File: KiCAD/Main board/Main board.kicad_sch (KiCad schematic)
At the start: 29 parts, among them J1 Conn_01x03, J10 Conn_01x03, J11 Conn_01x03, J12 Conn_01x03, J13 Conn_01x02, J14 Conn_01x02, J15 Conn_01x06, J16 Conn_01x02, J17 Conn_01x02, J18 Conn_01x05, J2 Conn_01x03, J3 Conn_01x02, J4 Conn_01x02, J5 Conn_01x03, J6 Conn_01x02, J7 Conn_01x03, J8 Conn_01x02, J9 Conn_01x03

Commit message: Ad good as finilized the main board schematic
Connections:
- net ADC_CH3_4/VU_G1_CH4: now reaches J18.2 (Pin_2)
- net ADC_CH3_4/VU_G2_CH4: now reaches J18.3 (Pin_3)
- net ADC_CH3_4/VU_O1_CH4: now reaches J18.4 (Pin_4)
- net ADC_CH3_4/VU_R1_CH4: now reaches J18.5 (Pin_5)
- net ADC_CH3_4/VU_G1_CH3: now reaches J18.2 (Pin_2)
- net ADC_CH3_4/VU_G2_CH3: now reaches J18.3 (Pin_3)
- net ADC_CH3_4/VU_O1_CH3: now reaches J18.4 (Pin_4)
- net ADC_CH3_4/VU_R1_CH3: now reaches J18.5 (Pin_5)
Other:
- sheet ADC_CH1_2 ports: added none; removed ~{RST_ADC_CH1_2}
- sheet ADC_CH3_4 ports: added BCK_ADC_CH3_4, DATA_ADC_CH3_4, LRCK_ADC_CH3_4, SCKI_ADC_CH3_4, VU_G1_CH3, VU_G1_CH4, VU_G2_CH3, VU_G2_CH4, VU_O1_CH3, VU_O1_CH4, VU_R1_CH3, VU_R1_CH4; removed none
- sheet FPGA ports: added BCK_ADC_CH3_4, DATA_ADC_CH3_4, LRCK_ADC_CH3_4, SCKI_ADC_CH3_4; removed ~{RST_ADC_CH1_2}
- note added: "-Use Panasonic ERA-8A series for audio path resistors -Use C0G MLCC capacitors for audio path capacitors"
- note added: "Check all custom symbols and footprints with someone else"
- moved on the sheet: H1, H2, H3, H4, H5, H6, H7, H8, J13, J14, J15

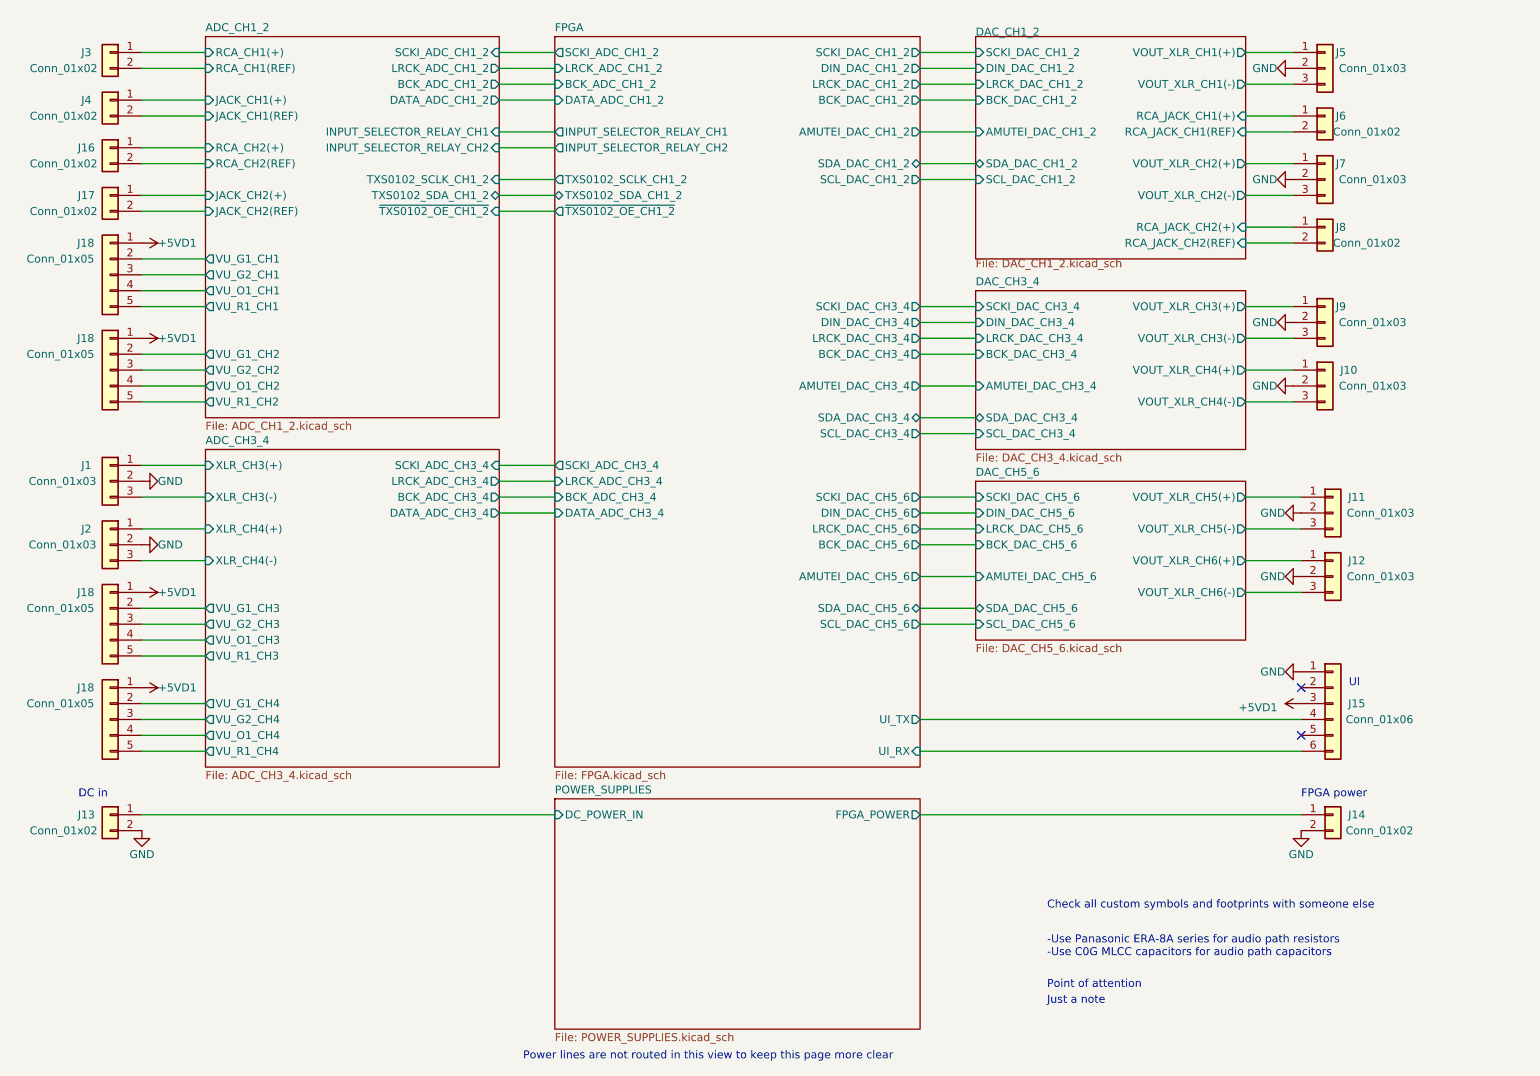
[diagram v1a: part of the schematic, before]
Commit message: Finalizer main board schematic exept passive order links. Schematic ready for review
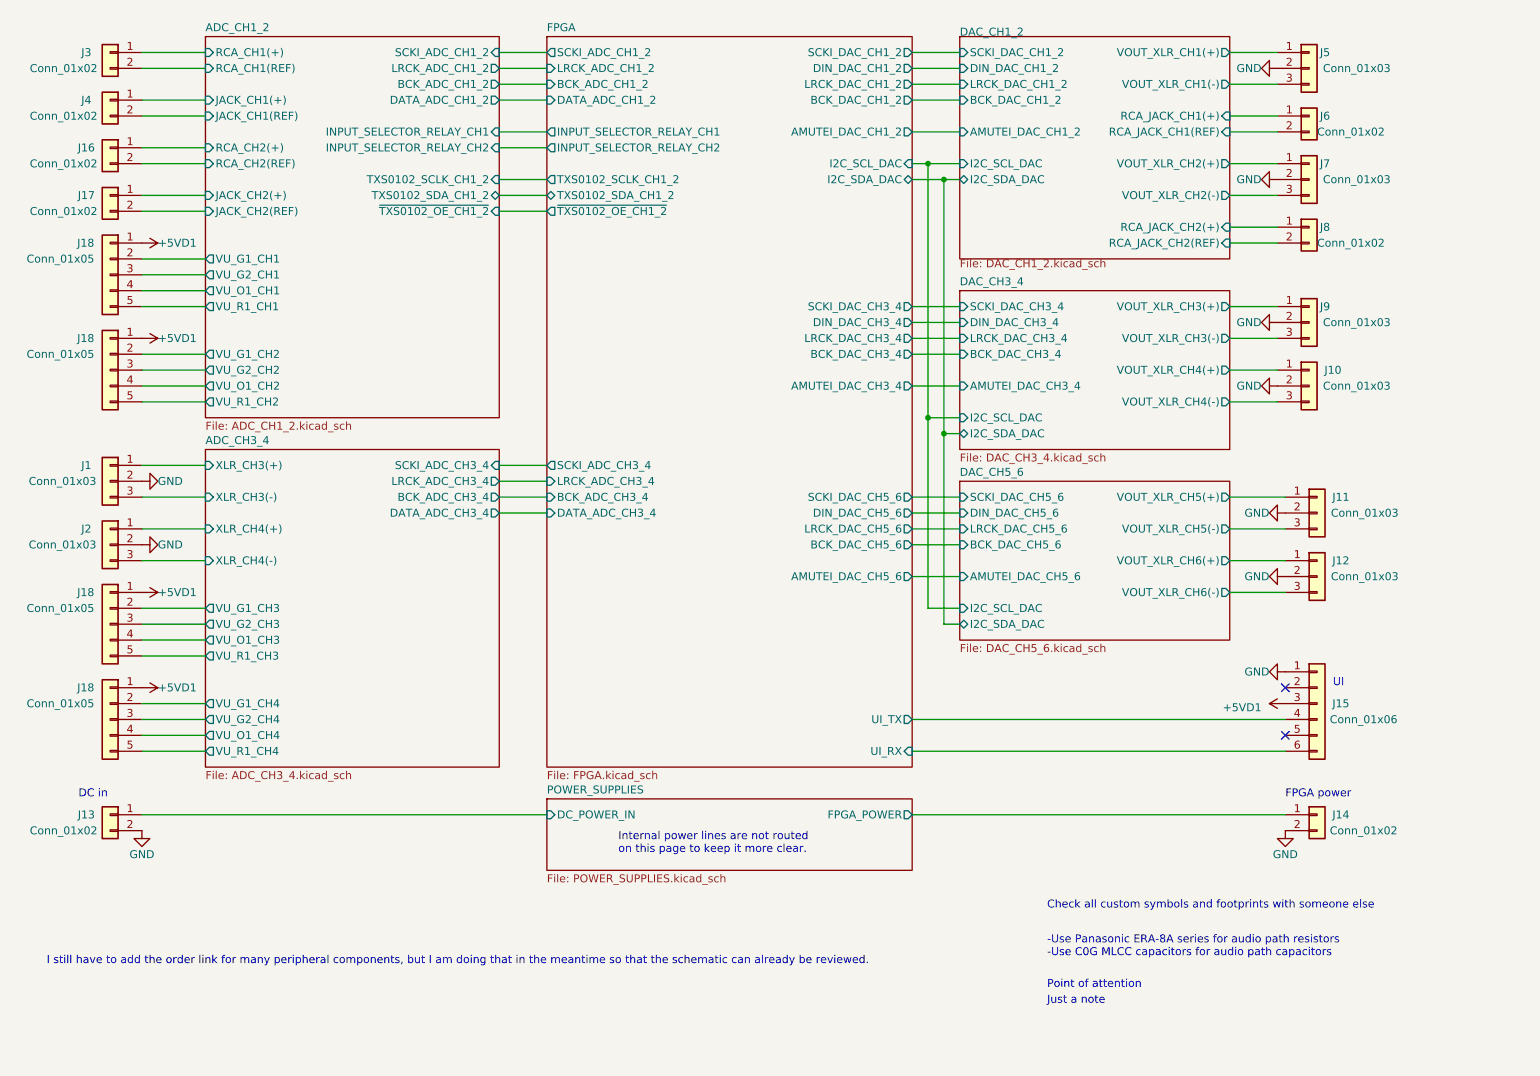
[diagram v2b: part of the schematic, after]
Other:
- sheet DAC_CH1_2 ports: added I2C_SCL_DAC, I2C_SDA_DAC; removed SCL_DAC_CH1_2, SDA_DAC_CH1_2
- sheet DAC_CH3_4 ports: added I2C_SCL_DAC, I2C_SDA_DAC; removed SCL_DAC_CH3_4, SDA_DAC_CH3_4
- sheet DAC_CH5_6 ports: added I2C_SCL_DAC, I2C_SDA_DAC; removed SCL_DAC_CH5_6, SDA_DAC_CH5_6
- sheet FPGA ports: added I2C_SCL_DAC, I2C_SDA_DAC; removed SCL_DAC_CH1_2, SCL_DAC_CH3_4, SCL_DAC_CH5_6, SDA_DAC_CH1_2, SDA_DAC_CH3_4, SDA_DAC_CH5_6
- note added: "I still have to add the order link for many peripheral components, but I am doing that in the meantime so that the schematic can already be reviewed."
- note added: "Internal power lines are not routed on this page to keep it more clear."
- note removed: "Power lines are not routed in this view to keep this page more clear"
- moved on the sheet: J10, J11, J12, J14, J15, J5, J6, J7, J8, J9

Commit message: Added component links to main board schematic
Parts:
- J1, J10, J11, J12, J16, J17, J2, J3, J4, J5, J6, J7, J8, J9: Cable (none) -> https://www.tinytronics.nl/shop/nl/kabels-en-connectoren/ka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
- J15: Cable (none) -> https://www.tinytronics.nl/shop/nl/kabels-en-connectoren/ka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; Datasheet cable https://www.tinytronics.nl/shop/nl/kabels-en-connectoren/ka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 -> (none)
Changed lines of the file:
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@@
       (effects (font (size 1.27 1.27)) hide)
     )
-    (property "Datasheet" "~" (at 27.94 87.63 0)
+    (property "Datasheet" "https://www.tinytronics.nl/shop/nl/kabels-en-connectoren/connectoren/jst-compatible/jst-ph-3p-compatible-printplaatconnector-male" (at 27.94 87.63 0)
+      (effects (font (size 1.27 1.27)) hide)
+    )
+    (property "Cable" "https://www.tinytronics.nl/shop/nl/kabels-en-connectoren/kabels-en-adapters/jst-compatible/jst-ph-3p-compatible-kabel-20cm" (at 27.94 87.63 0)
       (effects (font (size 1.27 1.27)) hide)
     )
@@
       (effects (font (size 1.27 1.27)) hide)
     )
-    (property "Datasheet" "~" (at 27.94 19.05 0)
+    (property "Datasheet" "https://www.tinytronics.nl/shop/nl/kabels-en-connectoren/connectoren/jst-compatible/jst-ph-2p-compatible-printplaatconnector-male" (at 27.94 19.05 0)
+      (effects (font (size 1.27 1.27)) hide)
+    )
+    (property "Cable" "https://www.tinytronics.nl/shop/nl/kabels-en-connectoren/kabels-en-adapters/jst-compatible/jst-2.0mm-connector-met-kabel-ph2.0-2-pins" (at 27.94 19.05 0)
       (effects (font (size 1.27 1.27)) hide)
     )
@@
       (effects (font (size 1.27 1.27)) hide)
     )
-    (property "Datasheet" "~" (at 219.71 62.23 0)
+    (property "Datasheet" "https://www.tinytronics.nl/shop/nl/kabels-en-connectoren/connectoren/jst-compatible/jst-ph-3p-compatible-printplaatconnector-male" (at 219.71 62.23 0)
+      (effects (font (size 1.27 1.27)) hide)
+    )
+    (property "Cable" "https://www.tinytronics.nl/shop/nl/kabels-en-connectoren/kabels-en-adapters/jst-compatible/jst-ph-3p-compatible-kabel-20cm" (at 219.71 62.23 0)
       (effects (font (size 1.27 1.27)) hide)
     )
@@
       (effects (font (size 1.27 1.27)) hide)
     )
-    (property "Datasheet" "~" (at 219.71 29.21 0)
+    (property "Datasheet" "https://www.tinytronics.nl/shop/nl/kabels-en-connectoren/connectoren/jst-compatible/jst-ph-2p-compatible-printplaatconnector-male" (at 219.71 29.21 0)
+      (effects (font (size 1.27 1.27)) hide)
+    )
+    (property "Cable" "https://www.tinytronics.nl/shop/nl/kabels-en-connectoren/kabels-en-adapters/jst-compatible/jst-2.0mm-connector-met-kabel-ph2.0-2-pins" (at 219.71 29.21 0)
       (effects (font (size 1.27 1.27)) hide)
     )
@@
       (effects (font (size 1.27 1.27)) hide)
     )
-    (property "Datasheet" "~" (at 27.94 97.79 0)
+    (property "Datasheet" "https://www.tinytronics.nl/shop/nl/kabels-en-connectoren/connectoren/jst-compatible/jst-ph-3p-compatible-printplaatconnector-male" (at 27.94 97.79 0)
+      (effects (font (size 1.27 1.27)) hide)
+    )
+    (property "Cable" "https://www.tinytronics.nl/shop/nl/kabels-en-connectoren/kabels-en-adapters/jst-compatible/jst-ph-3p-compatible-kabel-20cm" (at 27.94 97.79 0)
       (effects (font (size 1.27 1.27)) hide)
     )
@@
       (effects (font (size 1.27 1.27)) hide)
     )
-    (property "Datasheet" "~" (at 27.94 34.29 0)
+    (property "Datasheet" "https://www.tinytronics.nl/shop/nl/kabels-en-connectoren/connectoren/jst-compatible/jst-ph-2p-compatible-printplaatconnector-male" (at 27.94 34.29 0)
+      (effects (font (size 1.27 1.27)) hide)
+    )
+    (property "Cable" "https://www.tinytronics.nl/shop/nl/kabels-en-connectoren/kabels-en-adapters/jst-compatible/jst-2.0mm-connector-met-kabel-ph2.0-2-pins" (at 27.94 34.29 0)
       (effects (font (size 1.27 1.27)) hide)
     )
@@
       (effects (font (size 1.27 1.27)) hide)
     )
-    (property "Datasheet" "~" (at 219.71 39.37 0)
+    (property "Datasheet" "https://www.tinytronics.nl/shop/nl/kabels-en-connectoren/connectoren/jst-compatible/jst-ph-3p-compatible-printplaatconnector-male" (at 219.71 39.37 0)
+      (effects (font (size 1.27 1.27)) hide)
+    )
+    (property "Cable" "https://www.tinytronics.nl/shop/nl/kabels-en-connectoren/kabels-en-adapters/jst-compatible/jst-ph-3p-compatible-kabel-20cm" (at 219.71 39.37 0)
       (effects (font (size 1.27 1.27)) hide)
     )
@@
       (effects (font (size 1.27 1.27)) hide)
     )
-    (property "Datasheet" "~" (at 219.71 46.99 0)
+    (property "Datasheet" "https://www.tinytronics.nl/shop/nl/kabels-en-connectoren/connectoren/jst-compatible/jst-ph-2p-compatible-printplaatconnector-male" (at 219.71 46.99 0)
+      (effects (font (size 1.27 1.27)) hide)
+    )
+    (property "Cable" "https://www.tinytronics.nl/shop/nl/kabels-en-connectoren/kabels-en-adapters/jst-compatible/jst-2.0mm-connector-met-kabel-ph2.0-2-pins" (at 219.71 46.99 0)
       (effects (font (size 1.27 1.27)) hide)
     )
@@
       (effects (font (size 1.27 1.27)) hide)
     )
-    (property "Datasheet cable" "https://www.tinytronics.nl/shop/nl/kabels-en-connectoren/kabels-en-adapters/jst-compatible/kabel-voor-stappenmotor-4-pin-jst-xh-naar-6-pin-jst-ph-motoraansluiting-20cm" (at 220.98 123.19 0)
+    (property "Cable" "https://www.tinytronics.nl/shop/nl/kabels-en-connectoren/kabels-en-adapters/jst-compatible/kabel-voor-stappenmotor-4-pin-jst-xh-naar-6-pin-jst-ph-motoraansluiting-20cm" (at 220.98 123.19 0)
       (effects (font (size 1.27 1.27)) hide)
     )
@@
       (effects (font (size 1.27 1.27)) hide)
     )
-    (property "Datasheet" "~" (at 219.71 72.39 0)
+    (property "Datasheet" "https://www.tinytronics.nl/shop/nl/kabels-en-connectoren/connectoren/jst-compatible/jst-ph-3p-compatible-printplaatconnector-male" (at 219.71 72.39 0)
+      (effects (font (size 1.27 1.27)) hide)
+    )
+    (property "Cable" "https://www.tinytronics.nl/shop/nl/kabels-en-connectoren/kabels-en-adapters/jst-compatible/jst-ph-3p-compatible-kabel-20cm" (at 219.71 72.39 0)
       (effects (font (size 1.27 1.27)) hide)
     )
@@
       (effects (font (size 1.27 1.27)) hide)
     )
-    (property "Datasheet" "~" (at 220.98 102.87 0)
+    (property "Datasheet" "https://www.tinytronics.nl/shop/nl/kabels-en-connectoren/connectoren/jst-compatible/jst-ph-3p-compatible-printplaatconnector-male" (at 220.98 102.87 0)
+      (effects (font (size 1.27 1.27)) hide)
+    )
+    (property "Cable" "https://www.tinytronics.nl/shop/nl/kabels-en-connectoren/kabels-en-adapters/jst-compatible/jst-ph-3p-compatible-kabel-20cm" (at 220.98 102.87 0)
       (effects (font (size 1.27 1.27)) hide)
     )
@@
       (effects (font (size 1.27 1.27)) hide)
     )
-    (property "Datasheet" "~" (at 219.71 21.59 0)
+    (property "Datasheet" "https://www.tinytronics.nl/shop/nl/kabels-en-connectoren/connectoren/jst-compatible/jst-ph-3p-compatible-printplaatconnector-male" (at 219.71 21.59 0)
+      (effects (font (size 1.27 1.27)) hide)
+    )
+    (property "Cable" "https://www.tinytronics.nl/shop/nl/kabels-en-connectoren/kabels-en-adapters/jst-compatible/jst-ph-3p-compatible-kabel-20cm" (at 219.71 21.59 0)
       (effects (font (size 1.27 1.27)) hide)
     )
@@
       (effects (font (size 1.27 1.27)) hide)
     )
-    (property "Datasheet" "~" (at 220.98 92.71 0)
+    (property "Datasheet" "https://www.tinytronics.nl/shop/nl/kabels-en-connectoren/connectoren/jst-compatible/jst-ph-3p-compatible-printplaatconnector-male" (at 220.98 92.71 0)
+      (effects (font (size 1.27 1.27)) hide)
+    )
+    (property "Cable" "https://www.tinytronics.nl/shop/nl/kabels-en-connectoren/kabels-en-adapters/jst-compatible/jst-ph-3p-compatible-kabel-20cm" (at 220.98 92.71 0)
       (effects (font (size 1.27 1.27)) hide)
     )
@@
       (effects (font (size 1.27 1.27)) hide)
     )
-    (property "Datasheet" "~" (at 27.94 41.91 0)
+    (property "Datasheet" "https://www.tinytronics.nl/shop/nl/kabels-en-connectoren/connectoren/jst-compatible/jst-ph-2p-compatible-printplaatconnector-male" (at 27.94 41.91 0)
+      (effects (font (size 1.27 1.27)) hide)
+    )
+    (property "Cable" "https://www.tinytronics.nl/shop/nl/kabels-en-connectoren/kabels-en-adapters/jst-compatible/jst-2.0mm-connector-met-kabel-ph2.0-2-pins" (at 27.94 41.91 0)
       (effects (font (size 1.27 1.27)) hide)
     )
@@
       (effects (font (size 1.27 1.27)) hide)
     )
-    (property "Datasheet" "~" (at 27.94 26.67 0)
-      (effects (font (size 1.27 1.27)) hide)
-    )
+    (property "Datasheet" "https://www.tinytronics.nl/shop/nl/kabels-en-connectoren/connectoren/jst-compatible/jst-ph-2p-compatible-printplaatconnector-male" (at 27.94 26.67 0)
+      (effects (font (size 1.27 1.27)) hide)
+    )
+    (property "Cable" "https://www.tinytronics.nl/shop/nl/kabels-en-connectoren/kabels-en-adapters/jst-compatible/jst-2.0mm-connector-met-kabel-ph2.0-2-pins" (at 27.94 26.67 0)
+      (effects (font (size 1.27 1.27)) hide)
+    )

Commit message: Main board
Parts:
- J13: footprint Connector_Phoenix_MC:PhoenixContact_MCV_1,5_2-G-3.5_1x02_P3.50mm_Vertical -> Connector_Phoenix_MC:PhoenixContact_MCV_1,5_2-G-3.81_1x02_P3.81mm_Vertical; Wire housing (none) -> https://www.tinytronics.nl/shop/nl/kabels-en-connectoren/co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
- J14: FPGA connector (none) -> https://www.tinytronics.nl/shop/nl/kabels-en-connectoren/co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; Wire housing (none) -> https://www.tinytronics.nl/shop/nl/kabels-en-connectoren/co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
- J18: LEDs for all VU-meters (none) -> https://www.tinytronics.nl/shop/nl/componenten/led's/led's/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
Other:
- note added: "Let all custom symbols and footprints be checked by someone else to decrease the chance of errors."
- note added: "Panasonic ERA-8A series for audio path resistors C0G MLCC capacitors for audio path capacitors"
- note removed: "-Use Panasonic ERA-8A series for audio path resistors -Use C0G MLCC capacitors for audio path capacitors"
- note removed: "Check all custom symbols and footprints with someone else"
- note removed: "I still have to add the order link for many peripheral components, but I am doing that in the meantime so that the schematic can already be reviewed."
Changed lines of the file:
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@@
     (effects (font (size 1.27 1.27)) (justify left bottom))
   )
-  (text "Check all custom symbols and footprints with someone else"
-    (at 177.8 156.21 0)
-    (effects (font (size 1.27 1.27) (color 200 0 200 1)) (justify left bottom))
-  )
-  (text "I still have to add the order link for many peripheral components, but I am doing that in the meantime so that the schematic can already be reviewed."
-    (at 17.78 165.1 0)
-    (effects (font (size 1.27 1.27) (color 200 0 200 1)) (justify left bottom))
+  (text "Let all custom symbols and footprints be checked by someone else to decrease the chance of errors."
+    (at 72.39 158.75 0)
+    (effects (font (size 1.27 1.27) (thickness 0.254) bold (color 255 0 0 1)) (justify left bottom))
   )
   (text "DC in" (at 22.86 138.43 0)
@@
     (effects (font (size 1.27 1.27) (color 200 0 200 1)) (justify left bottom))
   )
-  (text "-Use Panasonic ERA-8A series for audio path resistors\n-Use C0G MLCC capacitors for audio path capacitors"
-    (at 177.8 163.83 0)
+  (text "Panasonic ERA-8A series for audio path resistors\nC0G MLCC capacitors for audio path capacitors"
+    (at 177.8 180.34 0)
     (effects (font (size 1.27 1.27)) (justify left bottom))
   )
@@
       (effects (font (size 1.27 1.27)) hide)
     )
-    (property "Datasheet" "~" (at 220.98 140.97 0)
+    (property "Datasheet" "https://www.tinytronics.nl/shop/nl/kabels-en-connectoren/connectoren/schroefterminals/terminal-block-voor-afneembare-schroefterminal-2p-3.81mm" (at 220.98 140.97 0)
+      (effects (font (size 1.27 1.27)) hide)
+    )
+    (property "Wire housing" "https://www.tinytronics.nl/shop/nl/kabels-en-connectoren/connectoren/schroefterminals/afneembare-schroefterminal-90-2p-3.81mm" (at 220.98 140.97 0)
+      (effects (font (size 1.27 1.27)) hide)
+    )
+    (property "FPGA connector" "https://www.tinytronics.nl/shop/nl/kabels-en-connectoren/connectoren/dc-jack/dc-jack-plastic-5.5mm-male-90-graden" (at 220.98 140.97 0)
       (effects (font (size 1.27 1.27)) hide)
     )
@@
       (effects (font (size 1.27 1.27)) (justify left))
     )
-    (property "Footprint" "Connector_Phoenix_MC:PhoenixContact_MCV_1,5_2-G-3.5_1x02_P3.50mm_Vertical" (at 27.94 140.97 0)
-      (effects (font (size 1.27 1.27)) hide)
-    )
-    (property "Datasheet" "~" (at 27.94 140.97 0)
+    (property "Footprint" "Connector_Phoenix_MC:PhoenixContact_MCV_1,5_2-G-3.81_1x02_P3.81mm_Vertical" (at 27.94 140.97 0)
+      (effects (font (size 1.27 1.27)) hide)
+    )
+    (property "Datasheet" "https://www.tinytronics.nl/shop/nl/kabels-en-connectoren/connectoren/schroefterminals/terminal-block-voor-afneembare-schroefterminal-2p-3.81mm" (at 27.94 140.97 0)
+      (effects (font (size 1.27 1.27)) hide)
+    )
+    (property "Wire housing" "https://www.tinytronics.nl/shop/nl/kabels-en-connectoren/connectoren/schroefterminals/afneembare-schroefterminal-90-2p-3.81mm" (at 27.94 140.97 0)
       (effects (font (size 1.27 1.27)) hide)
     )
@@
       (effects (font (size 1.27 1.27)) hide)
     )
+    (property "LEDs for all VU-meters" "https://www.tinytronics.nl/shop/nl/componenten/led's/led's/led-set-5mm-groen-rood-geel-30-stuks-diffuus" (at 27.94 54.61 0)
+      (effects (font (size 1.27 1.27)) hide)
+    )
